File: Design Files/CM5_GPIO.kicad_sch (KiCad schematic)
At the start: 16 parts, among them J14 Micro_SD_Card_Det, J5 Conn_01x04_MountingPin, U1 RT9742GGJ5

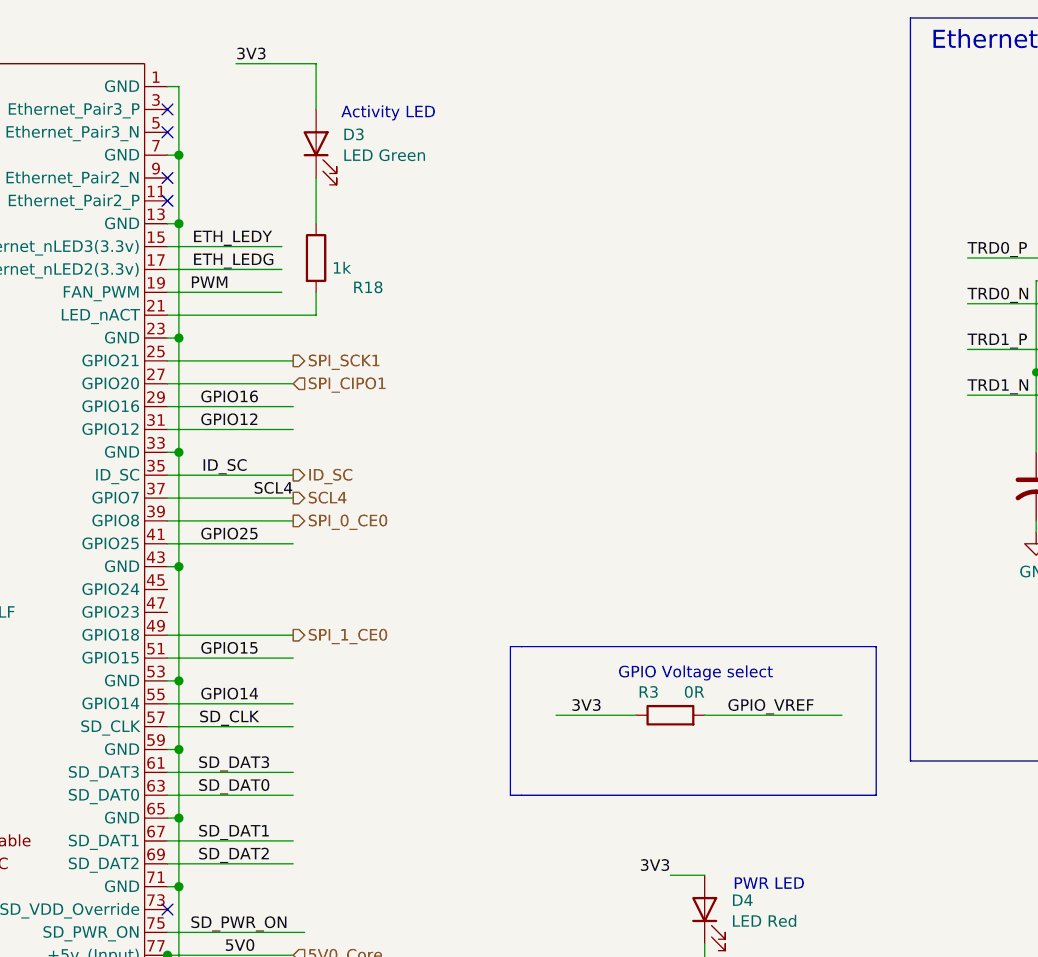
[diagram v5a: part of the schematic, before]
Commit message: SD pwr routed
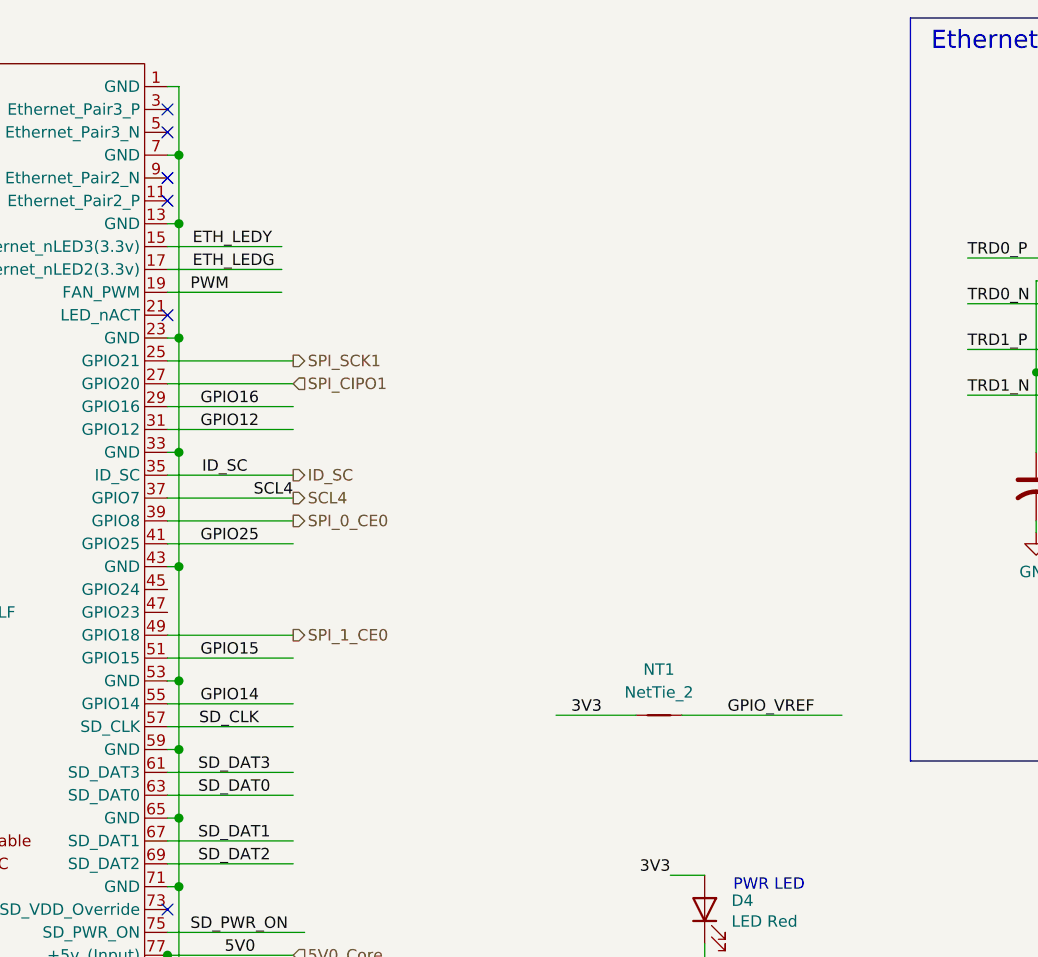
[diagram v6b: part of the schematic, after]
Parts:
- removed D3: LED Green, LED_SMD:LED_0603_1608Metric, symbol Device:LED
- removed R18: 1k, Resistor_SMD:R_0402_1005Metric, symbol Device:R
- removed R3: 0R, Resistor_SMD:R_0805_2012Metric_Pad1.20x1.40mm_HandSolder, symbol Device:R
- added NT1: NetTie_2, NetTie:NetTie-2_SMD_Pad0.5mm, symbol Device:NetTie_2
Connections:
- net 3V3_Peripheral: now also NT1.1
- net GPIO_VREF: now also NT1.2
- no-connect marks 17 -> 18
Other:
- note removed: "Activity LED"
- note removed: "GPIO Voltage select"
